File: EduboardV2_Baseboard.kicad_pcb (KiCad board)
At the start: 2 copper layers, 100 x 160 mm, 162 parts, among them IC201 PCF8563T_5,518, IC202 W25Q128JVSIQTR, IC301 XL1509-5.0E1, IC302 SY8113BADC, IC601 SP3485EN-L_TR, IC602 WM8782SEDS_RV_C323842, IC603 STK8321, IC604 CS4344-CZZ, IC605 STK8321, IC606 MCP9700AT-E_TT, J501 Conn_WS2812_Extern, Q301 AO3401A, Q302 AO3400A, Q303 AO3401A, Q304 AO3401A, SW301 1FS1T1B9M2RES-5, SW401 K2-1102SP-C4SC-04, SW402 K2-1102SP-C4SC-04, SW403 K2-1102SP-C4SC-04, SW404 K2-1102SP-C4SC-04, T401 AO3400A, T402 AO3400A, T403 AO3400A, T404 AO3400A, T405 AO3400A, T406 AO3400A, T501 AO3400A, T502 AO3400A, X201 PCIE-52P40H, X202 32.768 kHz, X203 TF-15×15, X204 CR1220-2ZX, X301 KF2EDGR-3.81-3P, X401 ER-TFT035-6, X501 USB3.1C16PFSMT, X502 BH-00105, X503 USB3.1C16PFSMT, X504 S4B-PH-SM4-K-TB(LF)(SN), X505 PJ-327C-4A, X506 PJ-327C-4A, X507 KF2EDGR-3.81-3P, X601 CH340G, Y601 X322512MSB4SI

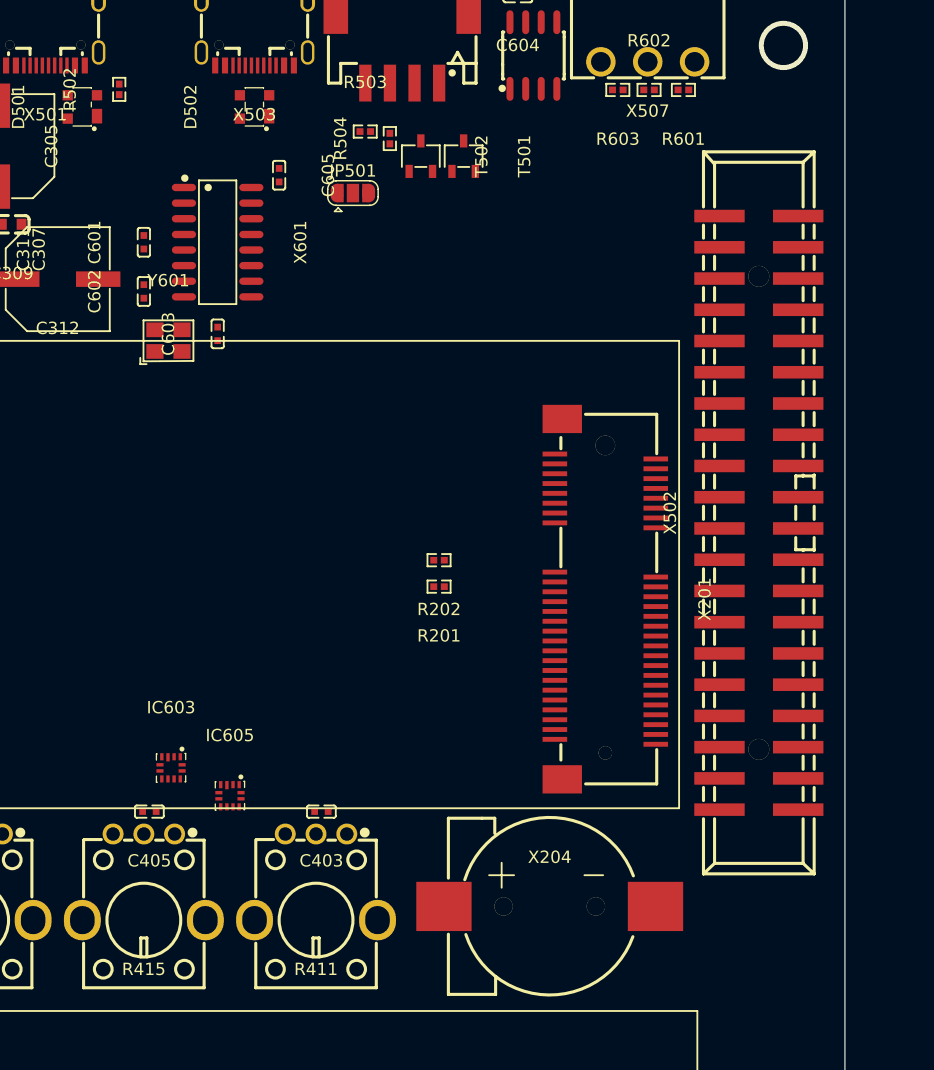
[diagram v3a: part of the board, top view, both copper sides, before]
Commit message: added rotary encoder
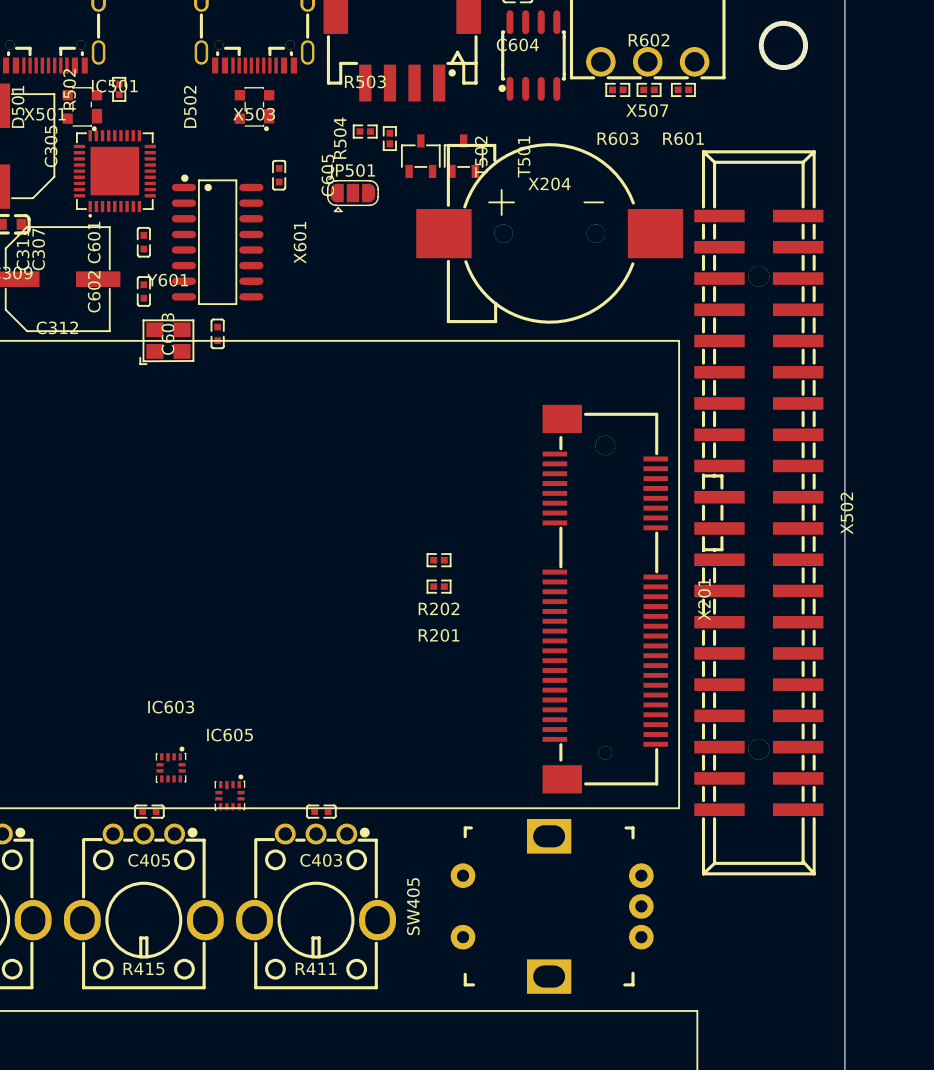
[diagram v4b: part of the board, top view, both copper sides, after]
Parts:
- added IC501: USB2514BI-AEZG-TR, eduboardv2:QFN-36_L6.0-W6.0-P0.50-BL-EP, F.Cu at (94.6, 36.2)
- added SW405: PEC11R-4220F-S0012, eduboardv2:SW-TH_PEC11R-4220F-S0012, F.Cu at (130.2, 96.0)
- moved X204 54.7 mm to (130.0, 41.3)
- turned X502 to -90 degrees
